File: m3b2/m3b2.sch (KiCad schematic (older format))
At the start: 28 parts, among them P6 MicroD-37Pins, Q1 MD3251, Q2 MD3251, U1 MC307, U10 MC308, U11 MC306, U14 MC308, U15 MC306, U19 MC302, U2 MC307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

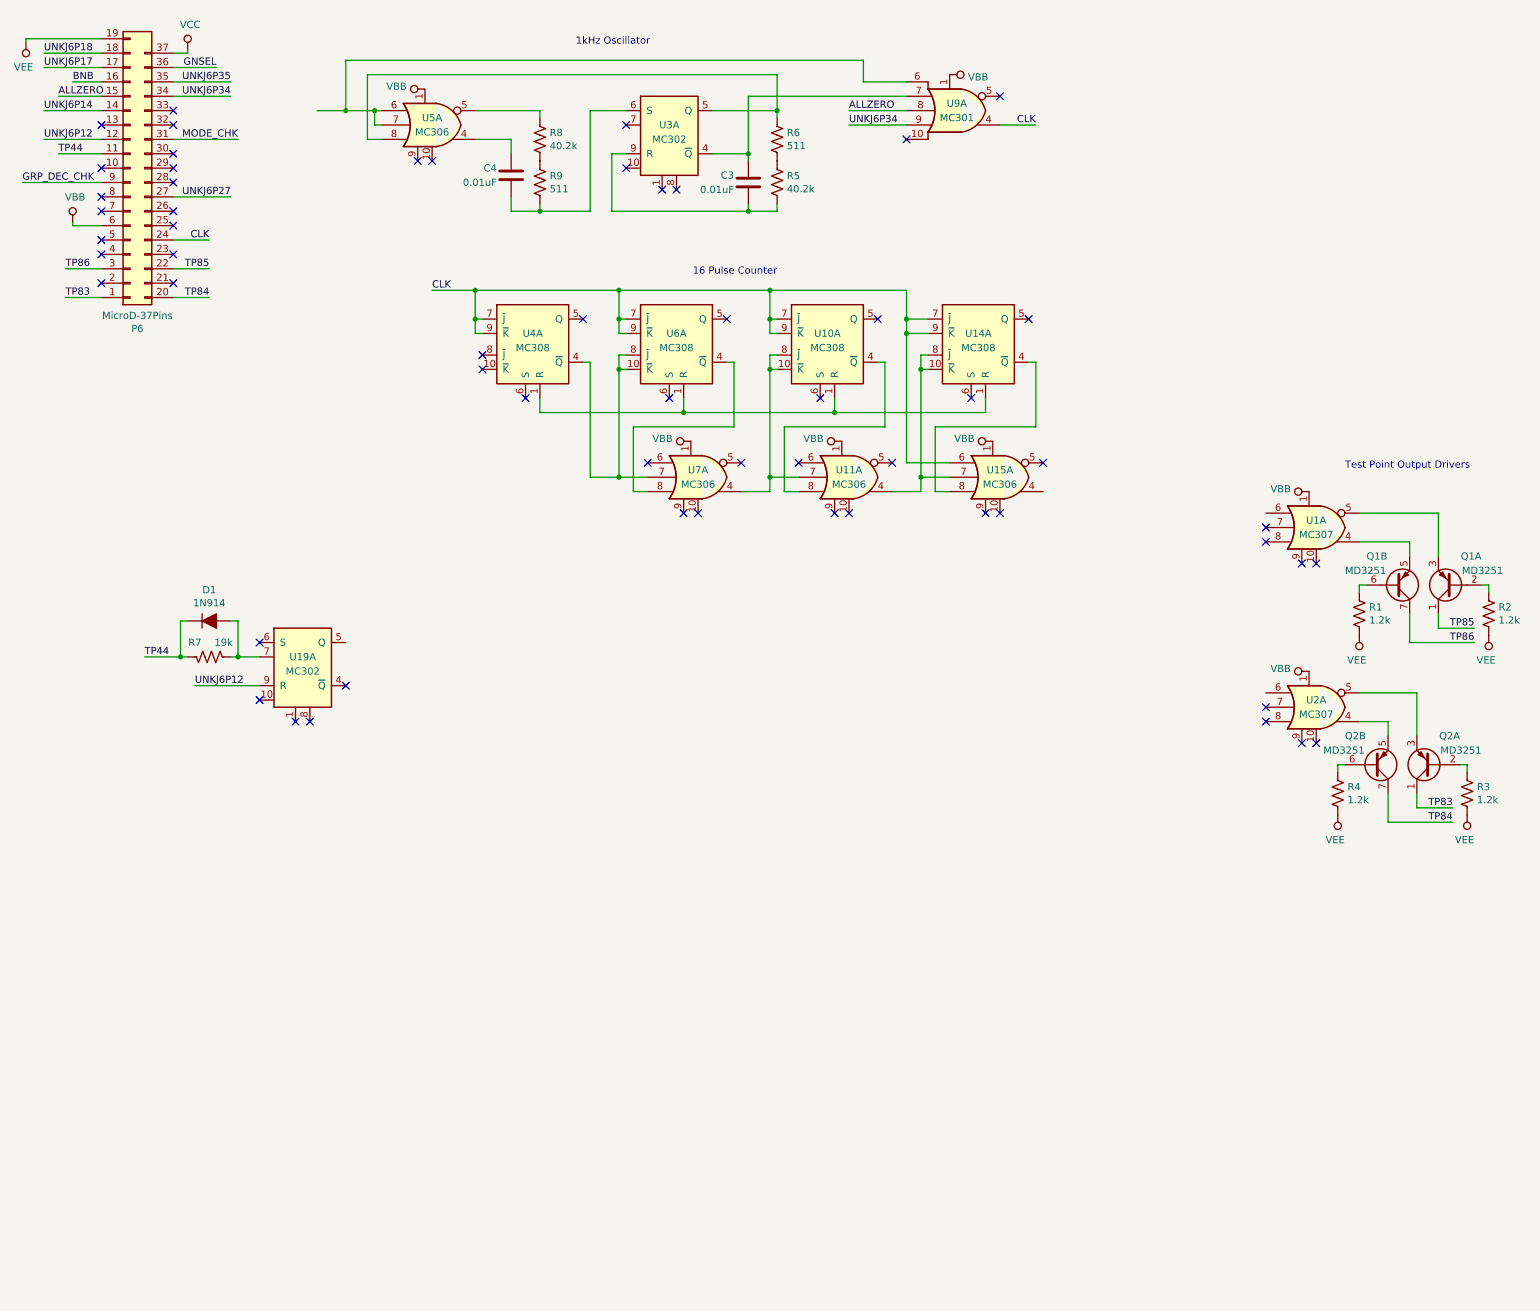
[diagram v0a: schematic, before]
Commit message: The module 3 board 2 schematic is now mostly complete, although it is a hangly tangly disaster.
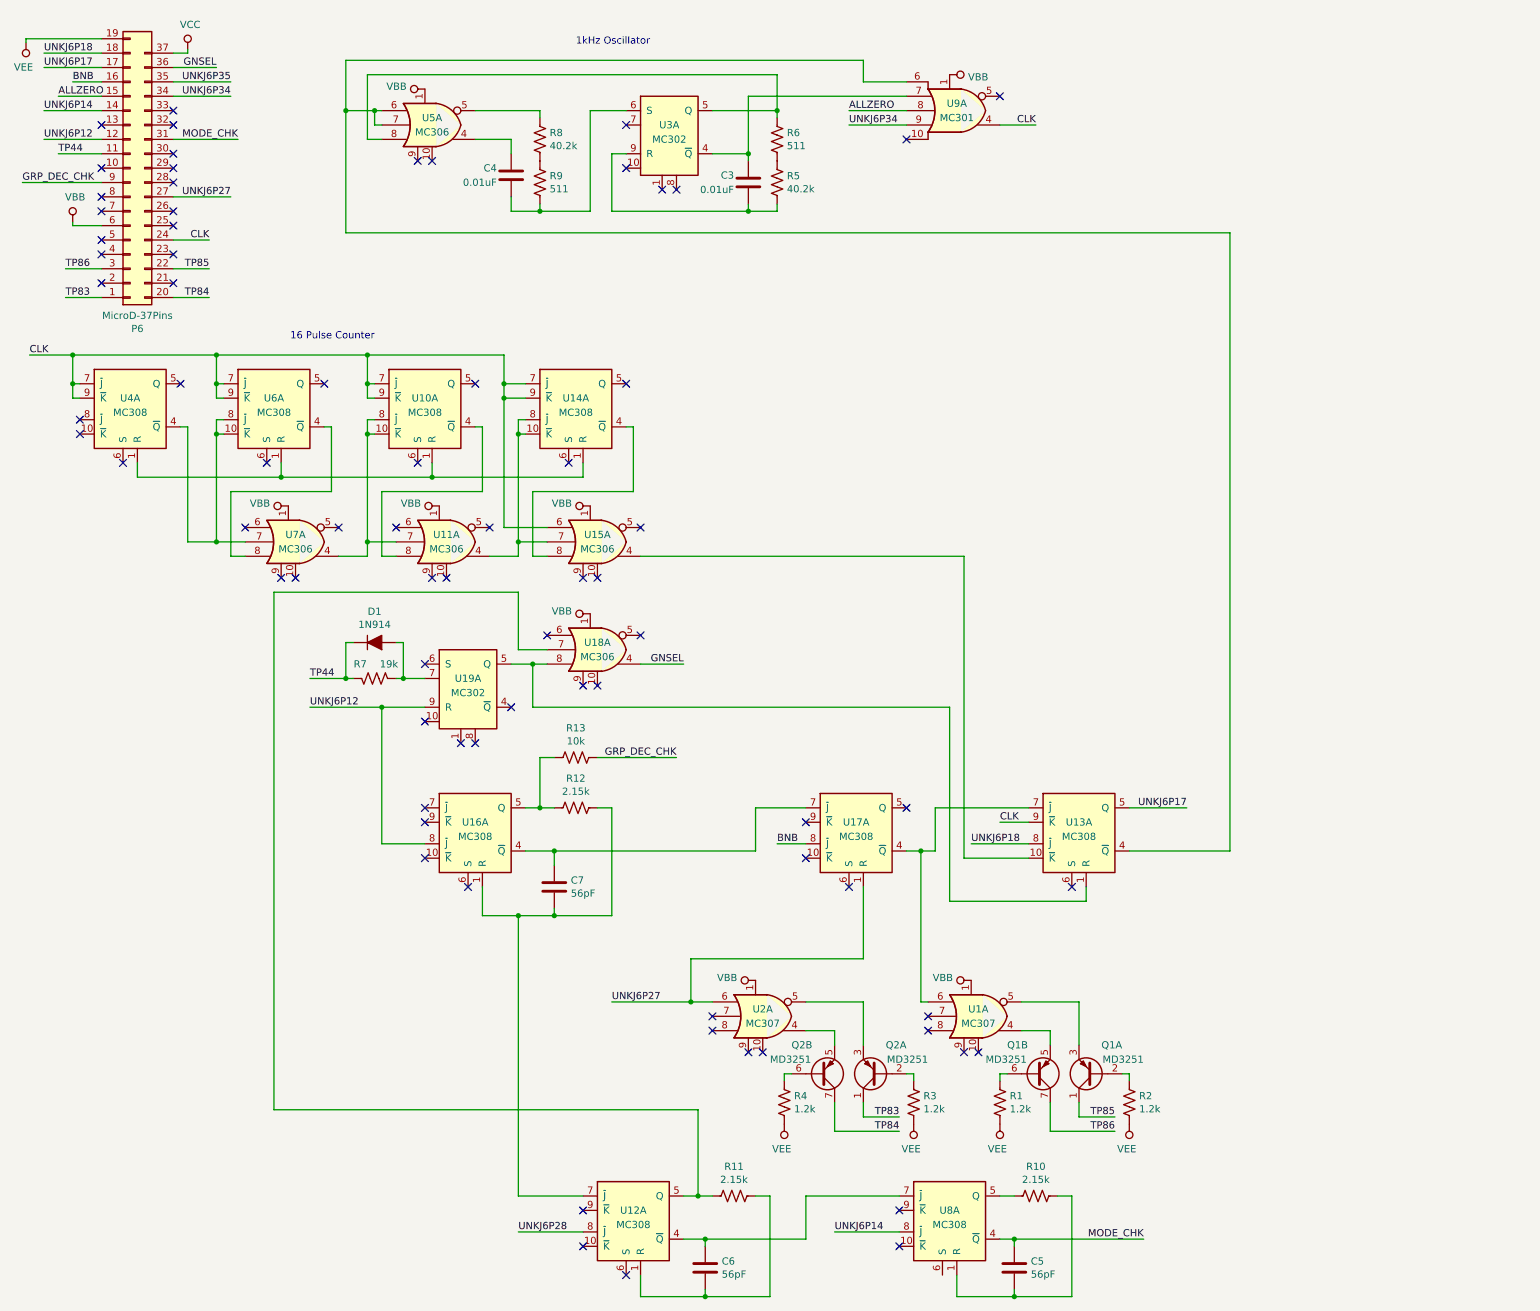
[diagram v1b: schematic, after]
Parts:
- added C5, C6, C7: 56pF, symbol Device:C
- added R10, R11, R12: 2.15k, symbol Device:R_US
- added R13: 10k, symbol Device:R_US
- added U12, U13, U16, U17, U8: MC308, symbol gn_buffer:MC308
- added U18: MC306, symbol gn_buffer:MC306
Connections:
- net BNB: now also U17.8 (~J)
- net CLK: now also U13.9 (~K)
- net GNSEL: now also U18.4
- net GRP_DEC_CHK: now also R13.1
- net MODE_CHK: now also C5.1, U8.4 (~Q)
- net UNKJ6P12: now also U16.8 (~J)
- net UNKJ6P14: now also U8.8 (~J)
- net UNKJ6P17: now also U13.5 (Q)
- net UNKJ6P18: now also U13.8 (~J)
- net UNKJ6P27: now also U2.6, U17.1 (R)
- net VBB: now also U18.1
- net at U5.6, U5.7, U9.6: now also U13.4 (~Q)
- net at U1.6: now also U13.7 (~J), U17.4 (~Q)
- net at U15.4: now also U13.10 (~K)
- net at U19.5 (Q): now also U13.1 (R), U18.8
- new net: R11.2, U12.5 (Q), U18.7
- new net: C7.2, R12.1, U12.7 (~J), U16.1 (R)
- new net: C7.1, U16.4 (~Q), U17.7 (~J)
- new net: R12.2, R13.2, U16.5 (Q)
- new net: C6.2, R11.1, U12.1 (R)
- new net: C6.1, U12.4 (~Q), U8.7 (~J)
- new net: C5.2, R10.1, U8.1 (R)
- new net: R10.2, U8.5 (Q)
- new net UNKJ6P28: U12.8 (~J)
- no-connect marks 58 -> 76
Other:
- note removed: "Test Point Output Drivers"
- moved on the sheet: D1, Q1A, Q1B, Q2A, Q2B, R1, R2, R3, R4, R7, U10A, U11A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

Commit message: Eradicated net names taken from ME901-0666 -- the pinout was completely changed from early revs of that document.
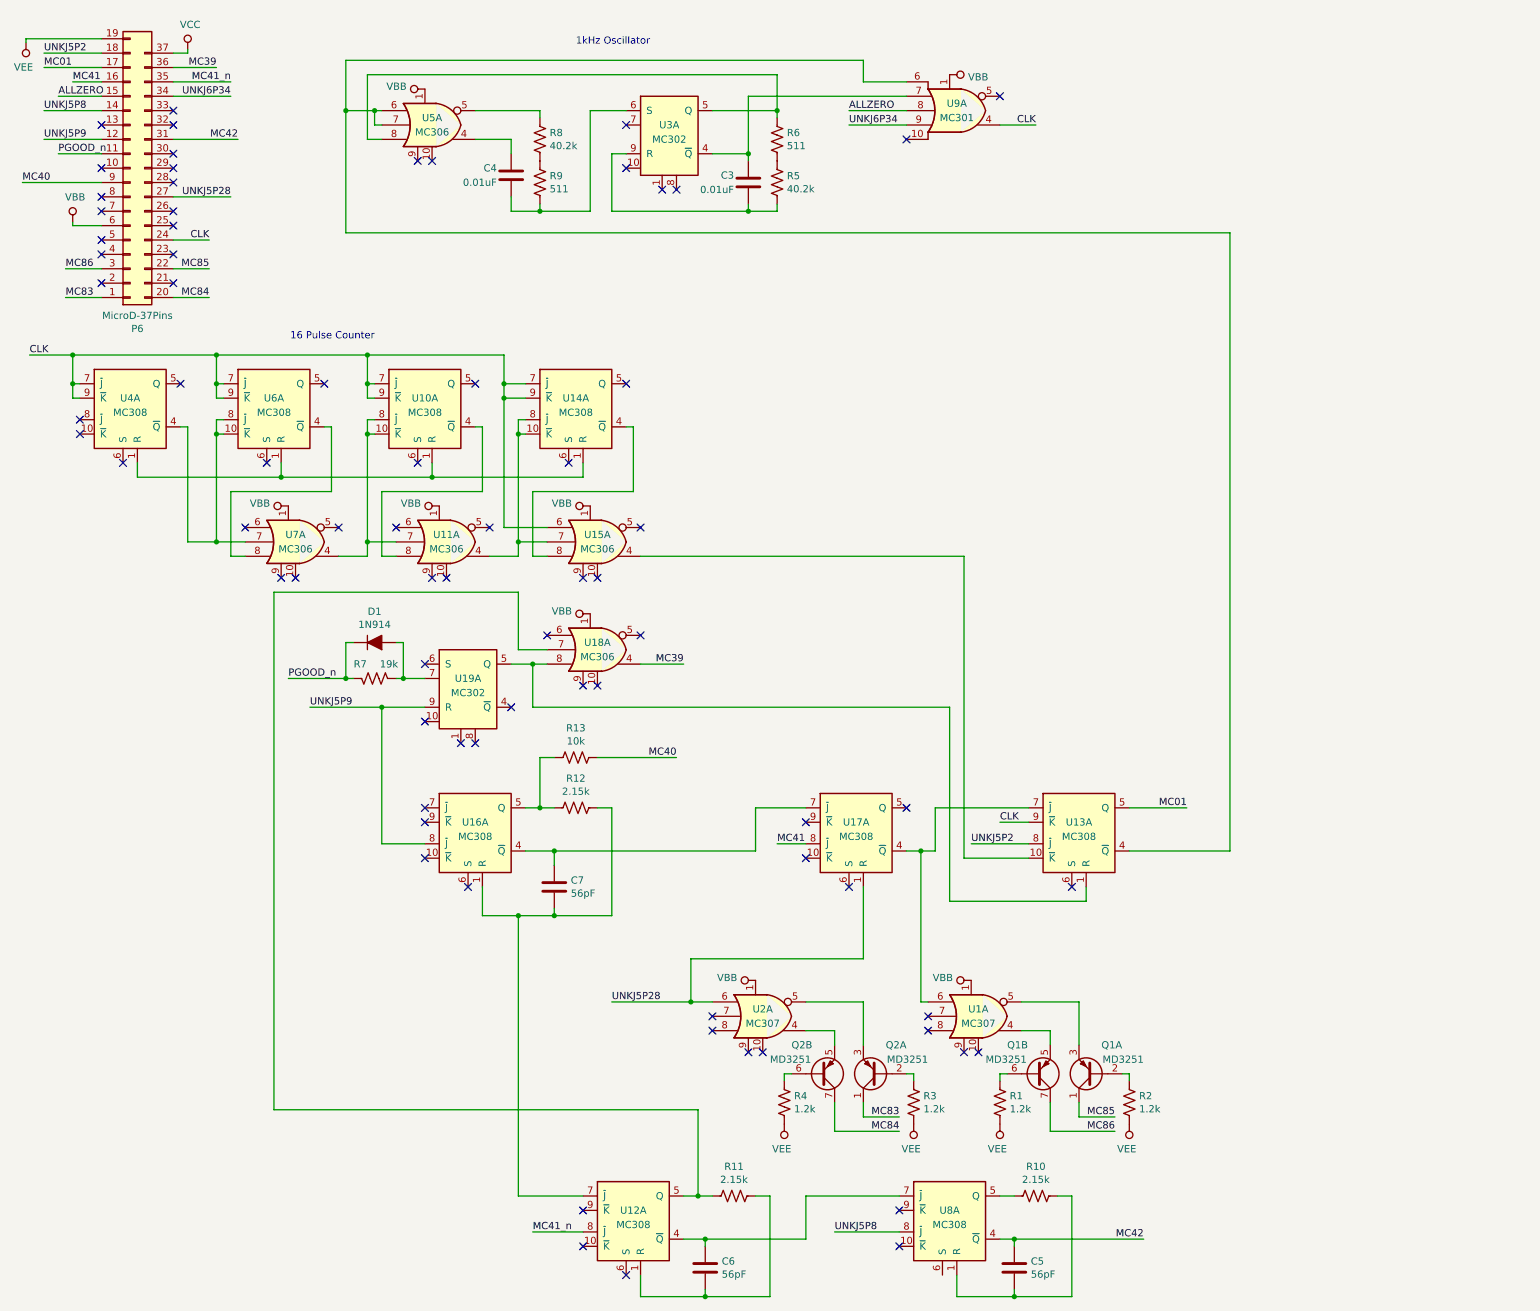
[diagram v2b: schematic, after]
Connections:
- net UNKJ6P35 is gone; now on net MC41_n: P6.35 (Pin_35)
- net BNB renamed MC41
- net GNSEL renamed MC39
- net GRP_DEC_CHK renamed MC40
- net MODE_CHK renamed MC42
- net TP44 renamed PGOOD_n
- net TP83 renamed MC83
- net TP84 renamed MC84
- net TP85 renamed MC85
- net TP86 renamed MC86
- net UNKJ6P12 renamed UNKJ5P9
- net UNKJ6P14 renamed UNKJ5P8
- net UNKJ6P17 renamed MC01
- net UNKJ6P18 renamed UNKJ5P2
- net UNKJ6P27 renamed UNKJ5P28
- net UNKJ6P28 renamed MC41_n
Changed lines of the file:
@@
 $EndComp
 Text Label 950  2350 0    50   ~ 0
-TP86
+MC86
 Wire Wire Line
 	1200 2350 950  2350
 Text Label 1950 2350 2    50   ~ 0
-TP85
+MC85
 Wire Wire Line
 	1700 2350 1950 2350
 Text Label 1950 2550 2    50   ~ 0
-TP84
+MC84
 Wire Wire Line
 	1700 2550 1950 2550
 Text Label 950  2550 0    50   ~ 0
-TP83
+MC83
 Wire Wire Line
 	1200 2550 950  2550
 Text Label 900  1550 0    50   ~ 0
-TP44
+PGOOD_n
 Wire Wire Line
 	1200 1550 900  1550
@@
 	2150 1450 1700 1450
 Text Label 2150 1450 2    50   ~ 0
-MODE_CHK
+MC42
 Text Label 1000 1050 0    50   ~ 0
-BNB
+MC41
 Wire Wire Line
 	1200 1050 1000 1050
 Text Label 2000 950  2    50   ~ 0
-GNSEL
+MC39
 Text Label 650  1750 0    50   ~ 0
-GRP_DEC_CHK
+MC40
 Wire Wire Line
 	1200 1750 650  1750
@@
 	1700 1850 2100 1850
 Text Label 2100 1850 2    50   ~ 0
-UNKJ6P27
+UNKJ5P28
 Wire Wire Line
 	1200 1450 800  1450
 Text Label 800  1450 0    50   ~ 0
-UNKJ6P12
+UNKJ5P9
 Wire Wire Line
 	1200 1250 800  1250
 Text Label 800  1250 0    50   ~ 0
-UNKJ6P14
+UNKJ5P8
 Wire Wire Line
 	1200 950  800  950
 Text Label 800  950  0    50   ~ 0
-UNKJ6P17
+MC01
 Wire Wire Line
 	1200 850  800  850
 Text Label 800  850  0    50   ~ 0
-UNKJ6P18
+UNKJ5P2
 Wire Wire Line
 	1700 1150 2100 1150
@@
 	1700 1050 2100 1050
 Text Label 2100 1050 2    50   ~ 0
-UNKJ6P35
+MC41_n
 $Comp
 L gn_buffer:MD3251 Q2
@@
 	6500 8250 6750 8250
 Text Label 6750 8250 2    50   ~ 0
-TP83
+MC83
 Text Label 6750 8350 2    50   ~ 0
-TP84
+MC84
 $Comp
 L gn_buffer:MD3251 Q1
@@
 	8000 8250 8250 8250
 Text Label 8250 8250 2    50   ~ 0
-TP85
+MC85
 Text Label 8250 8350 2    50   ~ 0
-TP86
+MC86
 $Comp
 L Device:R_US R4
@@
 $EndComp
 Text Label 5250 5100 2    50   ~ 0
-GNSEL
+MC39
 Wire Wire Line
 	4950 5100 5250 5100
@@
 Wire Wire Line
 	3150 5400 3150 6350
-Text Label 2650 5200 0    50   ~ 0
-TP44
+Text Label 2500 5200 0    50   ~ 0
+PGOOD_n
 Connection ~ 2900 5200
 Wire Wire Line
-	2900 5200 2650 5200
+	2900 5200 2500 5200
 Connection ~ 3300 5200
 Wire Wire Line
@@
 $EndComp
 Text Label 2650 5400 0    50   ~ 0
-UNKJ6P12
+UNKJ5P9
 Wire Wire Line
 	3450 5400 3150 5400
@@
 	6100 6350 5900 6350
 Text Label 5900 6350 0    50   ~ 0
-BNB
+MC41
 NoConn ~ 6400 6650
 Wire Wire Line
@@
 	5450 7450 5300 7450
 Text Label 4750 7450 0    50   ~ 0
-UNKJ6P27
+UNKJ5P28
 NoConn ~ 6800 6100
 Wire Wire Line
@@
 	7650 6350 7250 6350
 Text Label 7250 6350 0    50   ~ 0
-UNKJ6P18
+UNKJ5P2
 Wire Wire Line
 	8350 6100 8750 6100
 Text Label 8750 6100 2    50   ~ 0
-UNKJ6P17
+MC01
 Wire Wire Line
 	7000 6100 7650 6100
@@
 	4650 5750 5200 5750
 Text Label 5200 5750 2    50   ~ 0
-GRP_DEC_CHK
+MC40
 Wire Wire Line
 	4750 6100 4750 6850
@@
 NoConn ~ 4550 8900
 Wire Wire Line
-	4550 9050 4100 9050
-Text Label 4100 9050 0    50   ~ 0
-UNKJ6P28
+	4550 9050 4200 9050
+Text Label 4200 9050 0    50   ~ 0
+MC41_n
 Wire Wire Line
 	4100 6850 4100 8800
@@
 	6750 9050 6300 9050
 Text Label 6300 9050 0    50   ~ 0
-UNKJ6P14
+UNKJ5P8
 NoConn ~ 6750 8900
 NoConn ~ 6750 9150
@@
 Connection ~ 7550 9100
 Text Label 8450 9100 2    50   ~ 0
-MODE_CHK
+MC42
 $EndSCHEMATC

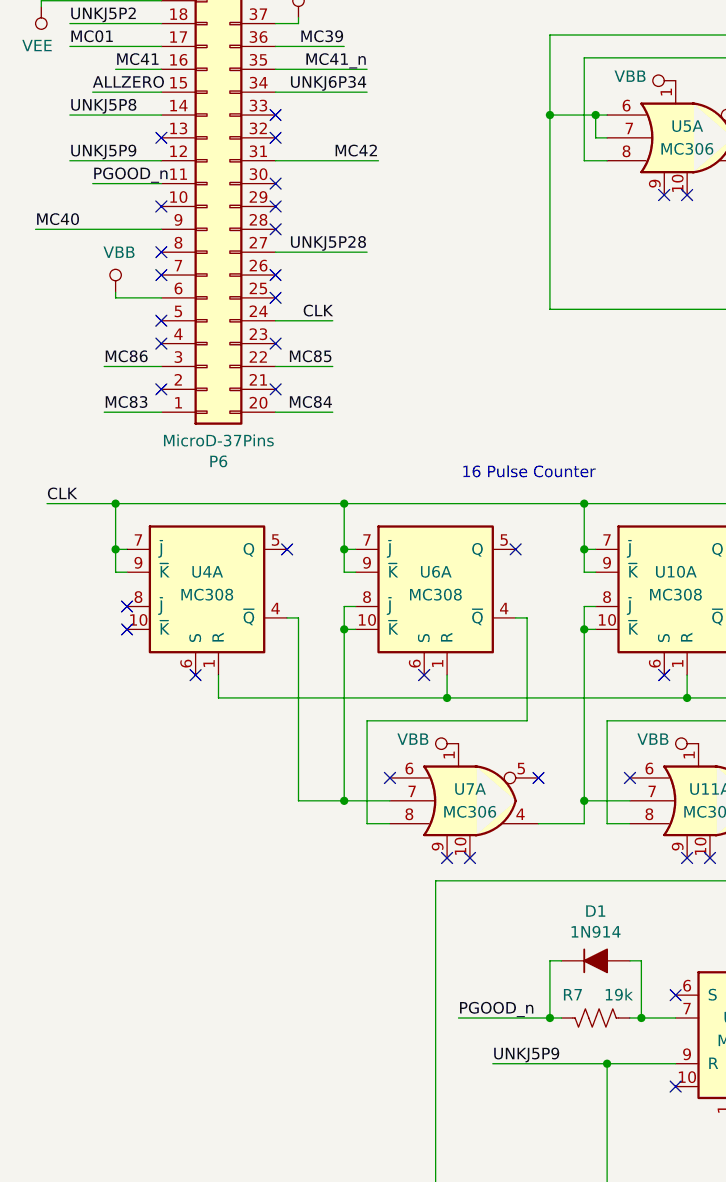
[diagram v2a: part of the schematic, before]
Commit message: Corrected a schematic error in module 3 board 1, which now makes much more sense. Also renamed the power good net to VFAIL.
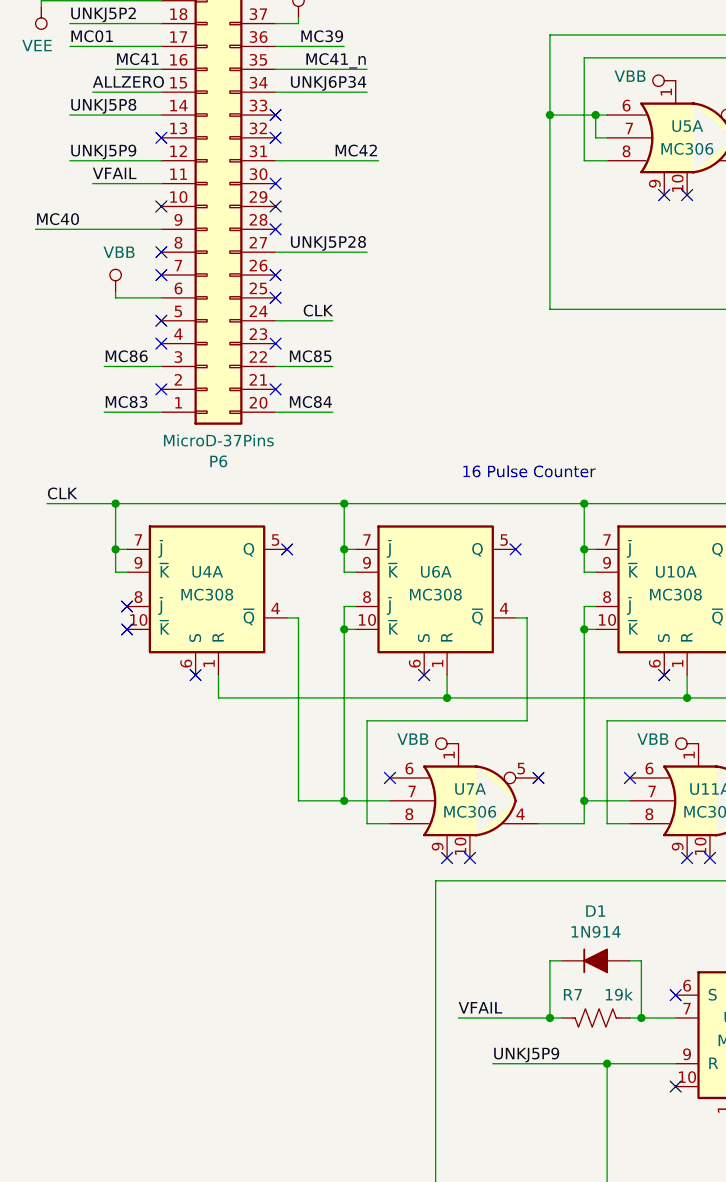
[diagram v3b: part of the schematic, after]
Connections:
- net PGOOD_n renamed VFAIL
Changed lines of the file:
@@
 	1200 2550 950  2550
 Text Label 900  1550 0    50   ~ 0
-PGOOD_n
+VFAIL
 Wire Wire Line
 	1200 1550 900  1550
@@
 	3150 5400 3150 6350
 Text Label 2500 5200 0    50   ~ 0
-PGOOD_n
+VFAIL
 Connection ~ 2900 5200
 Wire Wire Line
